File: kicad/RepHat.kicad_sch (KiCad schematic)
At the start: 4 parts, among them J1 GPIO, J13 Conn_01x03_Pin, J17 Screw_Terminal_01x02, J2 Screw_Terminal_01x02

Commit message: Miniaturizing the stepper drivers. They're still too big
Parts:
- J13: footprint Connector_JST:JST_XH_B3B-XH-A_1x03_P2.50mm_Vertical -> Connector_PinHeader_2.54mm:PinHeader_1x03_P2.54mm_Vertical
- J17, J2: footprint TerminalBlock_WAGO:TerminalBlock_WAGO_236-102_1x02_P5.00mm_45Degree -> TerminalBlock:TerminalBlock_bornier-2_P5.08mm
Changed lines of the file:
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@@
 			)
 		)
-		(property "Footprint" "TerminalBlock_WAGO:TerminalBlock_WAGO_236-102_1x02_P5.00mm_45Degree"
+		(property "Footprint" "TerminalBlock:TerminalBlock_bornier-2_P5.08mm"
 			(at 130.81 66.04 0)
 			(effects
@@
 			)
 		)
-		(property "Footprint" "TerminalBlock_WAGO:TerminalBlock_WAGO_236-102_1x02_P5.00mm_45Degree"
+		(property "Footprint" "TerminalBlock:TerminalBlock_bornier-2_P5.08mm"
 			(at 130.81 45.72 0)
 			(effects
@@
 			)
 		)
-		(property "Footprint" "Connector_JST:JST_XH_B3B-XH-A_1x03_P2.50mm_Vertical"
+		(property "Footprint" "Connector_PinHeader_2.54mm:PinHeader_1x03_P2.54mm_Vertical"
 			(at 158.75 41.91 0)
 			(effects

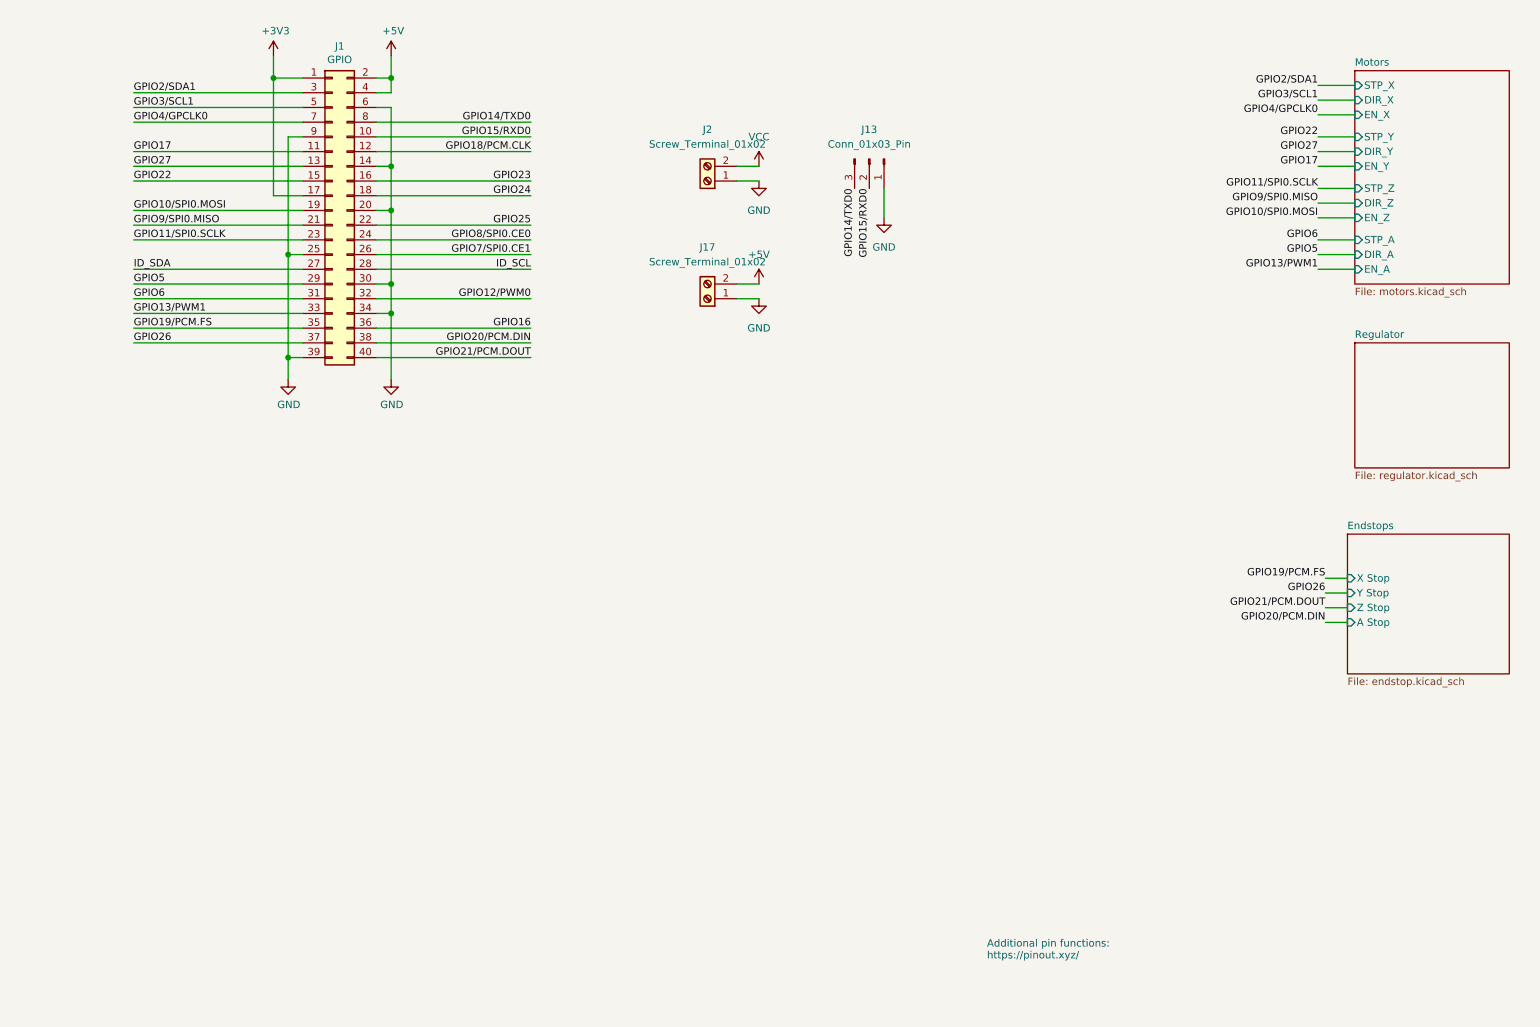
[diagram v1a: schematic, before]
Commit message: TMC2209->TMC2100, endstop protection optimization
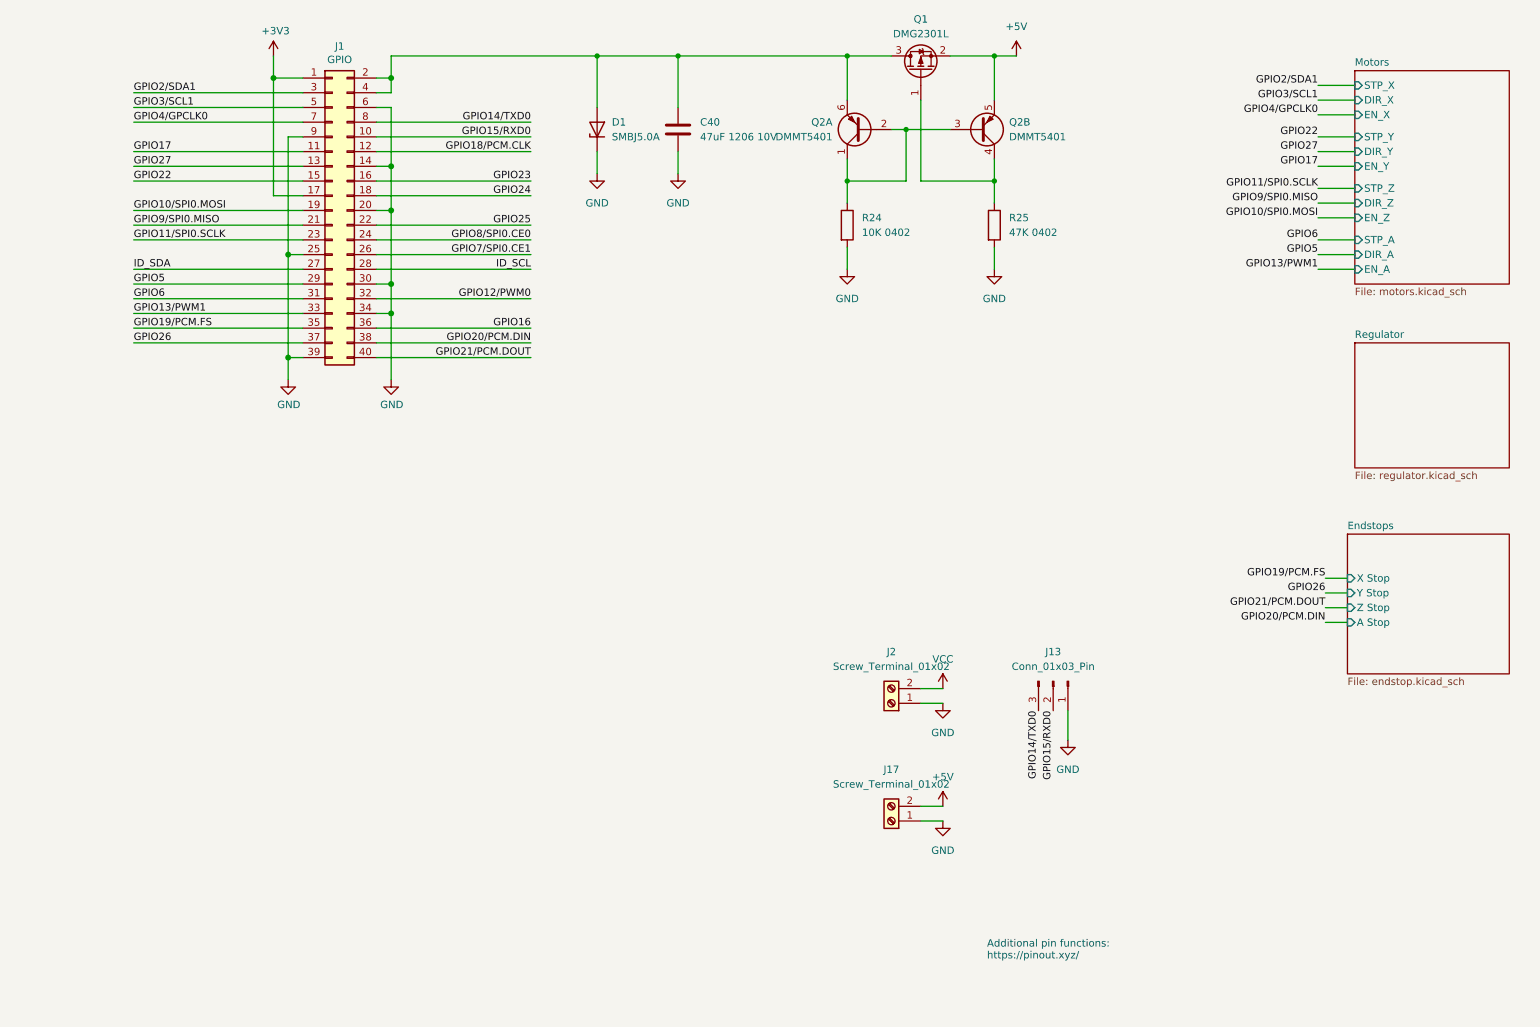
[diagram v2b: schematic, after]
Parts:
- added C40: 47uF 1206 10V, Capacitor_SMD:C_1206_3216Metric, symbol Device:C
- added D1: SMBJ5.0A, Diode_SMD:D_SMA-SMB_Universal_Handsoldering, symbol Device:D_Zener
- added Q1: DMG2301L, Package_TO_SOT_SMD:SOT-23, symbol Transistor_FET:DMG2301L
- added Q2: DMMT5401, Package_TO_SOT_SMD:SOT-23-6, symbol Transistor_BJT:DMMT5401
- added R24: 10K 0402, Resistor_SMD:R_0402_1005Metric, symbol Device:R
- added R25: 47K 0402, Resistor_SMD:R_0402_1005Metric, symbol Device:R
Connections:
- net +5V: now also Q1.2 (S), Q2.5 (E2); no longer J1.2 (Pin_2), J1.4 (Pin_4)
- net GND: now also C40.2, D1.1 (K), R24.2, R25.2
- new net: C40.1, D1.2 (A), J1.2 (Pin_2), J1.4 (Pin_4), Q1.3 (D), Q2.6 (E1)
- new net: Q2.1 (C1), Q2.2 (B1), Q2.3 (B2), R24.1
- new net: Q1.1 (G), Q2.4 (C2), R25.1
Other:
- moved on the sheet: J13, J17, J2

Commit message: schematic candidate 0
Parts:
- added C38: 0.1μF 0402 50V, Capacitor_SMD:C_0402_1005Metric, symbol Device:C
- added D4: SMBJ33A, Diode_SMD:D_SMB, symbol Device:D_Zener
- added D5: S8KC-13, Diode_SMD:D_SMC, symbol Device:D
- added F1: 3A, Fuse:Fuseholder_Littelfuse_Nano2_154x, symbol Device:Fuse
- added F2: 7A, Fuse:Fuseholder_Littelfuse_Nano2_154x, symbol Device:Fuse
- added F3: 1A, Fuse:Fuseholder_Littelfuse_Nano2_154x, symbol Device:Fuse
- added JP13: ID_WP, Jumper:SolderJumper-2_P1.3mm_Open_RoundedPad1.0x1.5mm, symbol Jumper:SolderJumper_2_Open
- added R10, R12: 3K9 0402, Resistor_SMD:R_0402_1005Metric, symbol Device:R
- added U7: M24C32-DFMN6TP, Package_SO:SOIC-8_5.275x5.275mm_P1.27mm, symbol Memory_EEPROM:CAT24C256
- D1: footprint Diode_SMD:D_SMA-SMB_Universal_Handsoldering -> Diode_SMD:D_SMB
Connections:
- net +3V3: now also C38.1, JP13.2 (B), R10.1, R12.1, U7.8 (VCC)
- net +5V: now also F1.2, F3.2; no longer J17.2 (Pin_2), Q1.2 (S), Q2.5 (E2)
- net GND: now also D1.2 (A), C38.2, D4.1 (K), D5.2 (A), U7.4 (GND); no longer D1.1 (K)
- net ID_SCL: now also R10.2, U7.6 (SCL)
- net ID_SDA: now also R12.2, U7.5 (SDA)
- net VCC: now also D5.1 (K), F2.2; no longer J2.2 (Pin_2)
- net at C40.1, J1.2 (Pin_2), J1.4 (Pin_4)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: now also D1.1 (K); no longer D1.2 (A)
- new net: F3.1, J17.2 (Pin_2)
- new net: JP13.1 (A), U7.7 (WP)
- new net: F1.1, Q1.2 (S), Q2.5 (E2)
- new net: D4.2 (A), F2.1, J2.2 (Pin_2)
- no-connect marks 0 -> 3
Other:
- note added: "12/24V in"
- note added: "3V3 UART"
- note added: "5V out"
- note added: "PI EEPROM"
- note removed: "Additional pin functions: https://pinout.xyz/"
- moved on the sheet: C40, D1, J1, J13, J17, J2, Q1, Q2A, Q2B, R24, R25

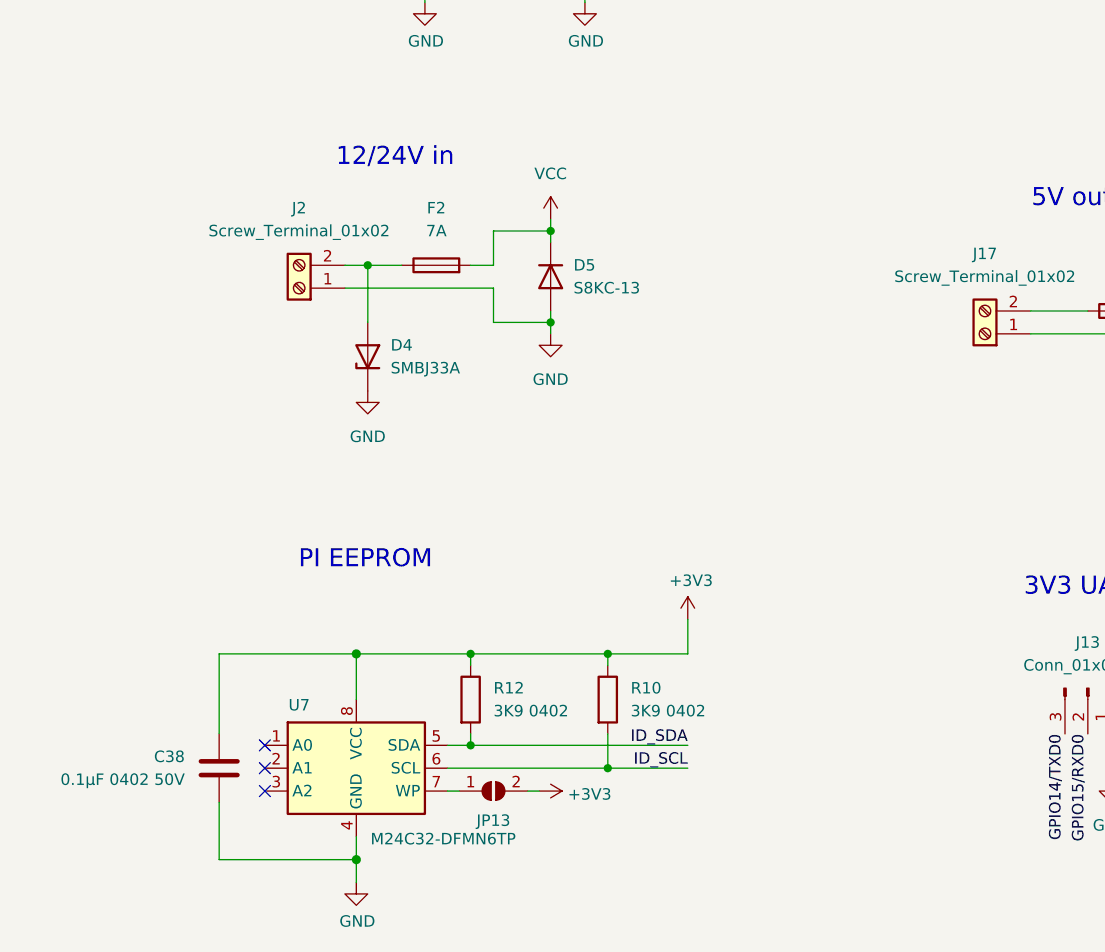
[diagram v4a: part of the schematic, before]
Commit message: new level shifter: bss138 transistors
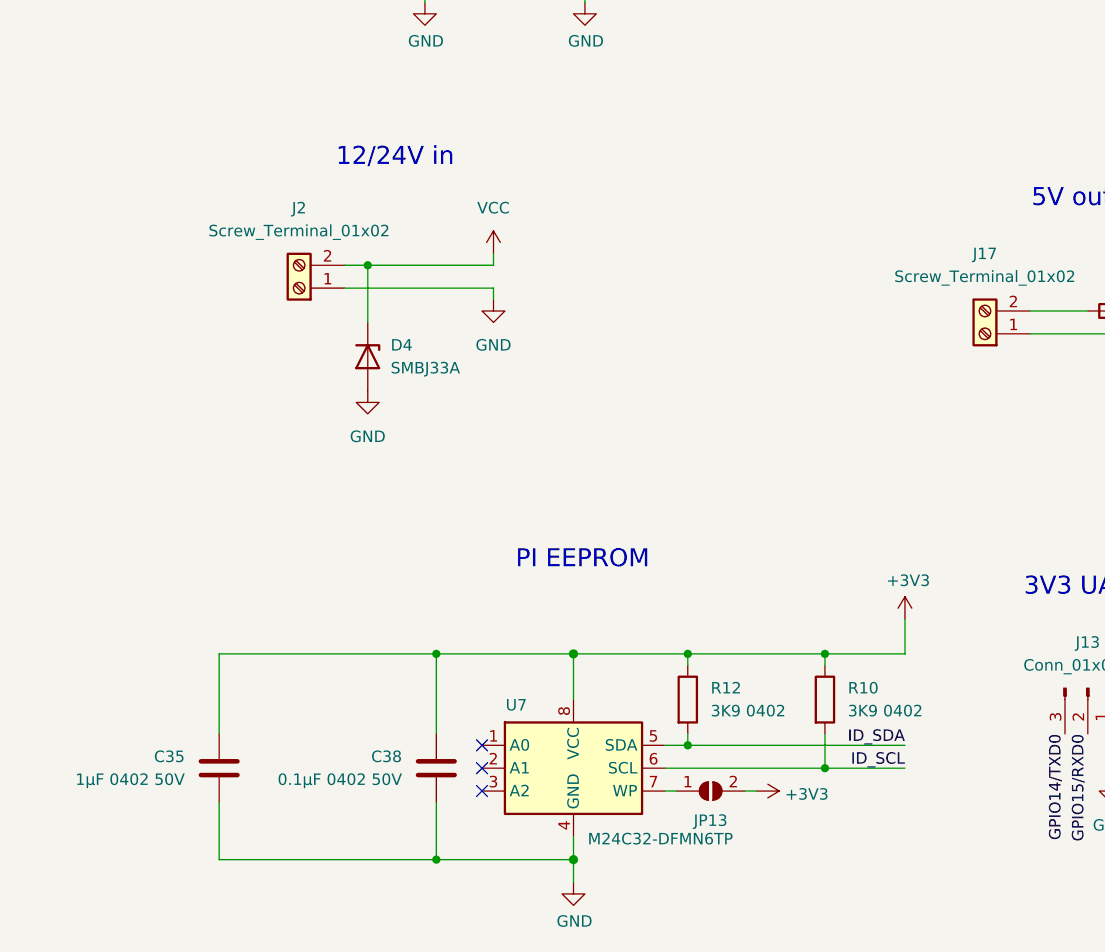
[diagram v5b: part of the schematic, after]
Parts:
- removed D5: S8KC-13, Diode_SMD:D_SMC, symbol Device:D
- removed F2: 7A, Fuse:Fuseholder_Littelfuse_Nano2_154x, symbol Device:Fuse
- added C35: 1μF 0402 50V, Capacitor_SMD:C_0402_1005Metric, symbol Device:C
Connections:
- net +3V3: now also C35.1
- net GND: now also D4.2 (A), C35.2; no longer D4.1 (K)
- net VCC: now also D4.1 (K), J2.2 (Pin_2)
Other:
- moved on the sheet: C38, D4, JP13, R10, R12, U7

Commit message: schematic finished
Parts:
- removed F3: 1A, Fuse:Fuseholder_Littelfuse_Nano2_154x, symbol Device:Fuse
- added F2: 1812L110 (1.1A), Fuse:Fuse_1812_4532Metric, symbol Device:Polyfuse
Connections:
- net +5V: now also F2.2
- net at J17.2 (Pin_2): now also F2.1
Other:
- moved on the sheet: J17
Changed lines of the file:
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@@
 	(wire
 		(pts
-			(xy 123.19 123.19) (xy 139.7 123.19)
-		)
-		(stroke
-			(width 0)
-			(type default)
-		)
-	)
-	(wire
-		(pts
 			(xy 100.33 171.45) (xy 109.22 171.45)
 		)
@@
 	(wire
 		(pts
-			(xy 123.19 120.65) (xy 129.54 120.65)
+			(xy 116.84 120.65) (xy 129.54 120.65)
 		)
 		(stroke
@@
 	(wire
 		(pts
+			(xy 116.84 123.19) (xy 144.78 123.19)
+		)
+		(stroke
+			(width 0)
+			(type default)
+		)
+	)
+	(wire
+		(pts
 			(xy 29.21 52.07) (xy 58.42 52.07)
 		)
@@
 	(wire
 		(pts
-			(xy 137.16 120.65) (xy 139.7 120.65)
-		)
-		(stroke
-			(width 0)
-			(type default)
-		)
-	)
-	(wire
-		(pts
 			(xy 73.66 39.37) (xy 71.12 39.37)
 		)
@@
 	(wire
 		(pts
+			(xy 137.16 120.65) (xy 144.78 120.65)
+		)
+		(stroke
+			(width 0)
+			(type default)
+		)
+	)
+	(wire
+		(pts
 			(xy 160.02 43.18) (xy 162.56 43.18)
 		)
@@
 	(symbol
 		(lib_id "Connector:Screw_Terminal_01x02")
-		(at 118.11 123.19 180)
+		(at 111.76 123.19 180)
 		(unit 1)
 		(exclude_from_sim no)
@@
 		(fields_autoplaced yes)
 		(property "Reference" "J17"
-			(at 118.11 114.3 0)
+			(at 111.76 114.3 0)
 			(effects
 				(font
@@
 		)
 		(property "Value" "Screw_Terminal_01x02"
-			(at 118.11 116.84 0)
+			(at 111.76 116.84 0)
 			(effects
 				(font
@@
 		)
 		(property "Footprint" "TerminalBlock:TerminalBlock_bornier-2_P5.08mm"
-			(at 118.11 123.19 0)
+			(at 111.76 123.19 0)
 			(effects
 				(font
@@
 		)
 		(property "Datasheet" "~"
-			(at 118.11 123.19 0)
+			(at 111.76 123.19 0)
 			(effects
 				(font
@@
 		)
 		(property "Description" ""
-			(at 118.11 123.19 0)
+			(at 111.76 123.19 0)
 			(effects
 				(font
@@
 	(symbol
 		(lib_id "power:GND")
-		(at 139.7 123.19 0)
+		(at 144.78 123.19 0)
 		(unit 1)
 		(exclude_from_sim no)
@@
 		(fields_autoplaced yes)
 		(property "Reference" "#PWR044"
-			(at 139.7 129.54 0)
+			(at 144.78 129.54 0)
 			(effects
 				(font
@@
 		)
 		(property "Value" "GND"
-			(at 139.7 128.27 0)
+			(at 144.78 128.27 0)
 			(effects
 				(font
@@
 		)
 		(property "Footprint" ""
-			(at 139.7 123.19 0)
+			(at 144.78 123.19 0)
 			(effects
 				(font
@@
 		)
 		(property "Datasheet" ""
-			(at 139.7 123.19 0)
+			(at 144.78 123.19 0)
 			(effects
 				(font
@@
 		)
 		(property "Description" ""
-			(at 139.7 123.19 0)
+			(at 144.78 123.19 0)
 			(effects
 				(font
@@
 	)
 	(symbol
+		(lib_id "Device:Polyfuse")
+		(at 133.35 120.65 90)
+		(unit 1)
+		(exclude_from_sim no)
+		(in_bom yes)
+		(on_board yes)
+		(dnp no)
+		(fields_autoplaced yes)
+		(property "Reference" "F2"
+			(at 133.35 114.3 90)
+			(effects
+				(font
+					(size 1.27 1.27)
+				)
+			)
+		)
+		(property "Value" "1812L110 (1.1A)"
+			(at 133.35 116.84 90)
+			(effects
+				(font
+					(size 1.27 1.27)
+				)
+			)
+		)
+		(property "Footprint" "Fuse:Fuse_1812_4532Metric"
+			(at 138.43 119.38 0)
+			(effects
+				(font
+					(size 1.27 1.27)
+				)
+				(justify left)
+				(hide yes)
+			)
+		)
+		(property "Datasheet" "https://www.littelfuse.com/media?resourcetype=datasheets&itemid=ca5c80cb-504e-4a8a-8e74-0107520a1717&filename=1812l-datasheet-update"
+			(at 133.35 120.65 0)
+			(effects
+				(font
+					(size 1.27 1.27)
+				)
+				(hide yes)
+			)
+		)
+		(property "Description" "Resettable fuse, polymeric positive temperature coefficient"
+			(at 133.35 120.65 0)
+			(effects
+				(font
+					(size 1.27 1.27)
+				)
+				(hide yes)
+			)
+		)
+		(pin "1"
+		)
+		(pin "2"
+		)
+		(instances
+			(project ""
+				(path "/e63e39d7-6ac0-4ffd-8aa3-1841a4541b55"
+					(reference "F2")
+					(unit 1)
+				)
+			)
+		)
+	)
+	(symbol
 		(lib_name "GND_1")
 		(lib_id "power:GND")
@@
 		(lib_name "+5V_1")
 		(lib_id "power:+5V")
-		(at 139.7 120.65 0)
+		(at 144.78 120.65 0)
 		(unit 1)
 		(exclude_from_sim no)
@@
 		(fields_autoplaced yes)
 		(property "Reference" "#PWR043"
-			(at 139.7 124.46 0)
+			(at 144.78 124.46 0)
 			(effects
 				(font
@@
 		)
 		(property "Value" "+5V"
-			(at 139.7 115.57 0)
+			(at 144.78 115.57 0)
 			(effects
 				(font
@@
 		)
 		(property "Footprint" ""
-			(at 139.7 120.65 0)
+			(at 144.78 120.65 0)
 			(effects
 				(font
@@
 		)
 		(property "Datasheet" ""
-			(at 139.7 120.65 0)
+			(at 144.78 120.65 0)
 			(effects
 				(font
@@
 		)
 		(property "Description" ""
-			(at 139.7 120.65 0)
+			(at 144.78 120.65 0)
 			(effects
 				(font
@@
 					(unit 1)
 				)
-			)
-		)
-	)
-	(symbol
-		(lib_id "Device:Fuse")
-		(at 133.35 120.65 90)
-		(unit 1)
-		(exclude_from_sim no)
-		(in_bom yes)
-		(on_board yes)
-		(dnp no)
-		(fields_autoplaced yes)
-		(property "Reference" "F3"
-			(at 133.35 114.3 90)
-			(effects
-				(font
-					(size 1.27 1.27)
-				)
-			)
-		)
-		(property "Value" "1A"
-			(at 133.35 116.84 90)
-			(effects
-				(font
-					(size 1.27 1.27)
-				)
-			)
-		)
-		(property "Footprint" "Fuse:Fuseholder_Littelfuse_Nano2_154x"
-			(at 133.35 122.428 90)
-			(effects
-				(font
-					(size 1.27 1.27)
-				)
-				(hide yes)
-			)
-		)
-		(property "Datasheet" "~"
-			(at 133.35 120.65 0)
-			(effects
-				(font
-					(size 1.27 1.27)
-				)
-				(hide yes)
-			)
-		)
-		(property "Description" "Fuse"
-			(at 133.35 120.65 0)
-			(effects
-				(font
-					(size 1.27 1.27)
-				)
-				(hide yes)
-			)
-		)
-		(pin "2"
-		)
-		(pin "1"
-		)
-		(instances
-			(project "RepHat"
-				(path "/e63e39d7-6ac0-4ffd-8aa3-1841a4541b55"
-					(reference "F3")
-					(unit 1)
-				)
